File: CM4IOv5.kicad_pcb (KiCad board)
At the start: 4 copper layers, 115.1 x 56 mm, 120 parts, among them J1 Conn_01x02, J10 HDMI_C_1.4, J11 HDMI_C_1.4, J13 Conn_01x03, J14 Conn_01x03, J15 Audio OUT, J16 Micro_SD_Card_Det, J17 THD-20-R, J2 Bus_M.2_Socket_B, J3 USB_OTG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

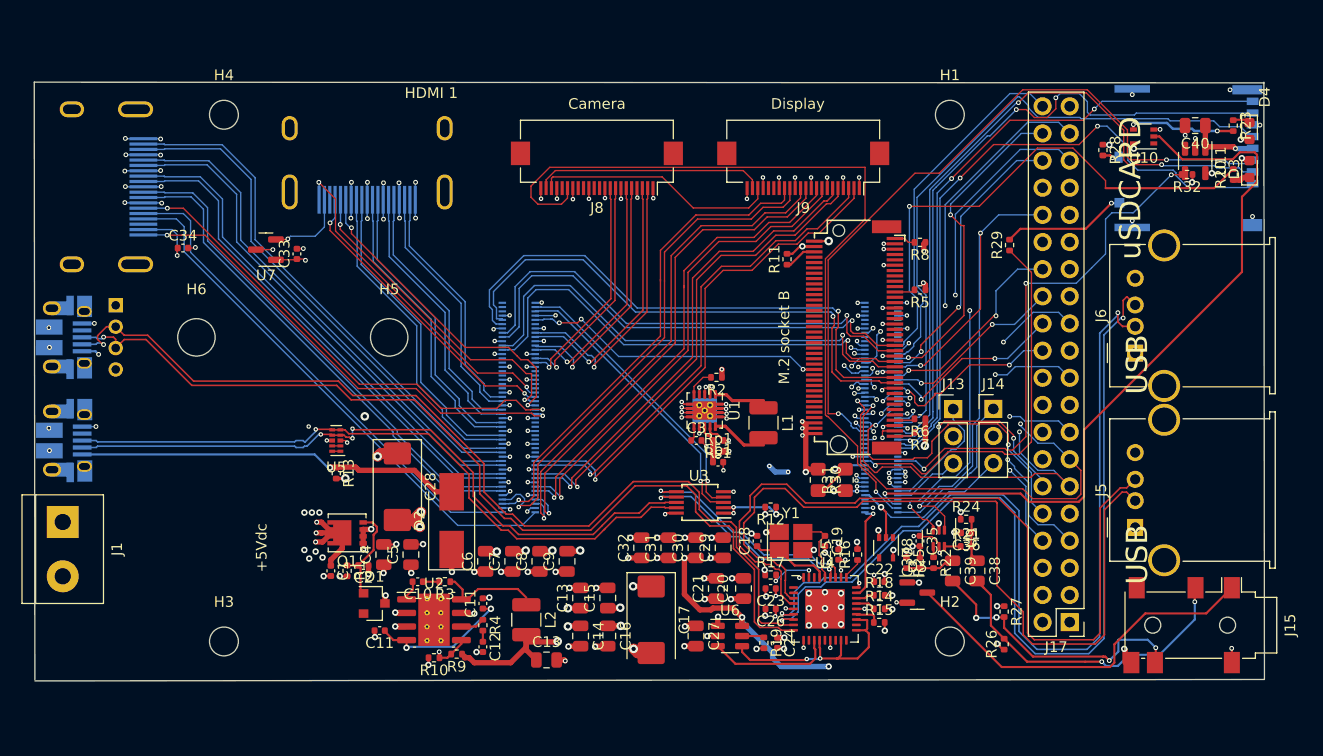
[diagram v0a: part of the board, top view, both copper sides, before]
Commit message: Completed initial routing
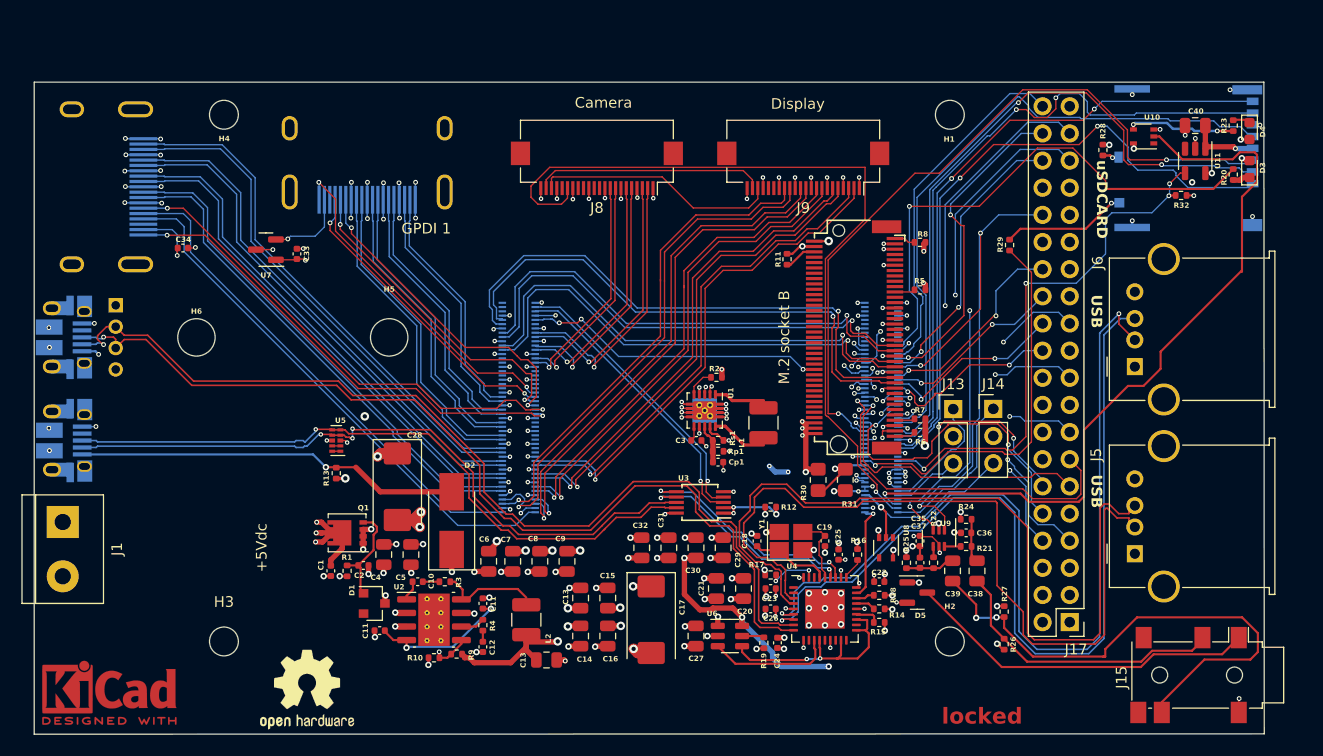
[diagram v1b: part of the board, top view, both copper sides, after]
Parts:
- added REF**: OSHW-Logo2_9.8x8mm_SilkScreen, Symbol:OSHW-Logo2_9.8x8mm_SilkScreen, F.Cu at (122.3, 135.8)
- added REF**: KiCad-Logo2_5mm_Copper, Symbol:KiCad-Logo2_5mm_Copper, F.Cu at (103.8, 136.1)
- moved J15 4.71 mm to (204.8, 134.4)
- moved J5 2.46 mm to (199.8, 123.1)
- moved R32 2.04 mm to (204.1, 89.6)
- moved J6 1.27 mm to (199.8, 105.6)
- moved C6 0.29 mm to (139.3, 123.8)
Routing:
- net /CM4_GPIO (GPIO, SDCARD)/AUDIO_R: track 26.7 -> 49.1 mm, vias 4 -> 2
- net /CM4_GPIO (GPIO, SDCARD)/GPIO17: track 35.2 -> 27.3 mm, vias 2 -> 1
- net /CM4_GPIO (GPIO, SDCARD)/GPIO27: track 38.8 -> 32.8 mm, vias 2 -> 1
- net /+3.3v: track 327.0 -> 322.7 mm, vias 36 -> 37
- net /CM4_GPIO (GPIO, SDCARD)/AUDIO_L: track 31.0 -> 27.9 mm, vias 2 -> 0
- net (no net): track 2.65 -> 0.00 mm
- net Net-(D5-K): track 35.5 -> 33.2 mm
- net /USB2-HUB/HD3_P: track 84.3 -> 82.2 mm, vias 2 -> 1
- net /USB2-HUB/VBUS: track 165.0 -> 162.9 mm
- net /CM4_GPIO (GPIO, SDCARD)/SD_PWR_ON: track 49.1 -> 50.6 mm, vias 3 -> 4
- net /CM4_GPIO (GPIO, SDCARD)/nPWR_LED: track 70.5 -> 71.5 mm
- net /CM4_GPIO (GPIO, SDCARD)/SYNC_IN: track 0.94 -> 0.00 mm, vias 1 -> 0
- net Net-(D2-A): track 36.6 -> 36.1 mm
- net GND: track 184.1 -> 184.2 mm, vias 203 -> 193
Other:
- board size 115.1 x 56 mm -> 115.1 x 61 mm
- board text added: "GPDI 1"
- board text added: "locked"
- board text removed: "HDMI 1"

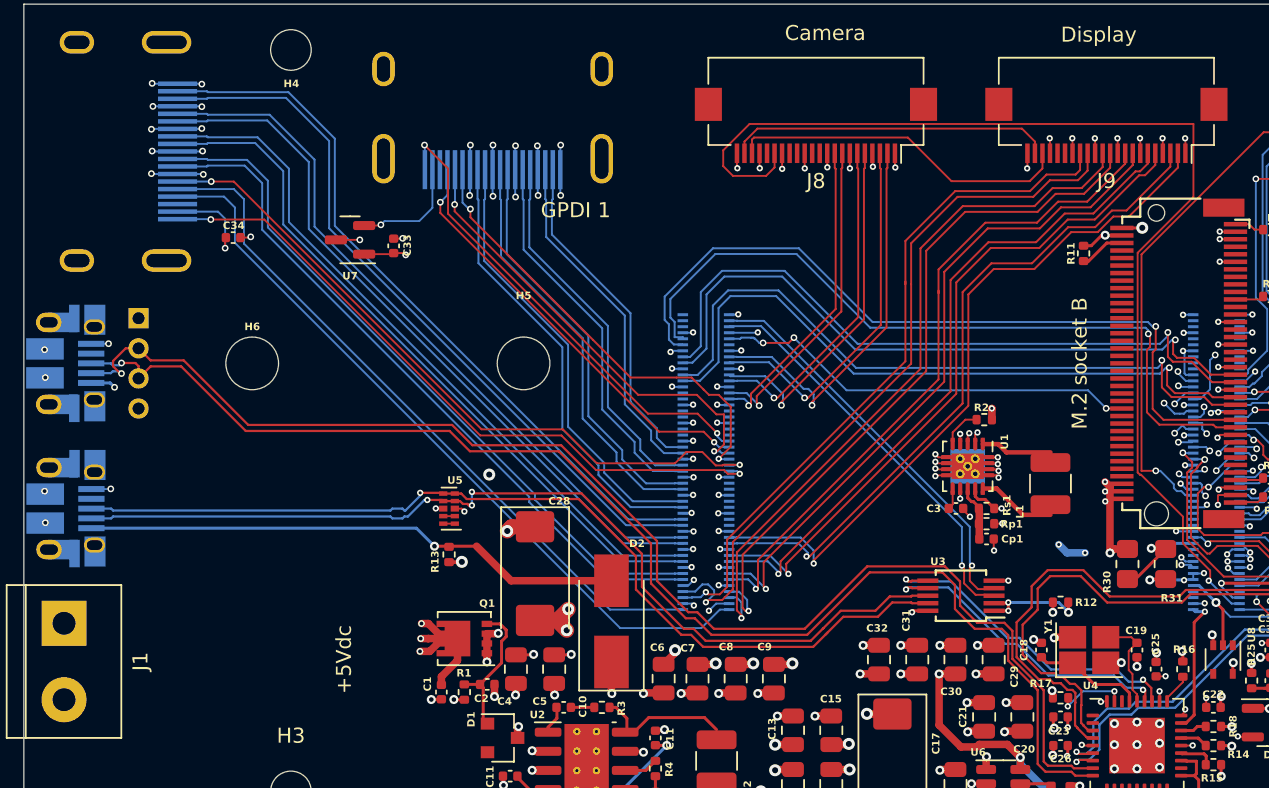
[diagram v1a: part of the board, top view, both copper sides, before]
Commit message: Tuning differential signals
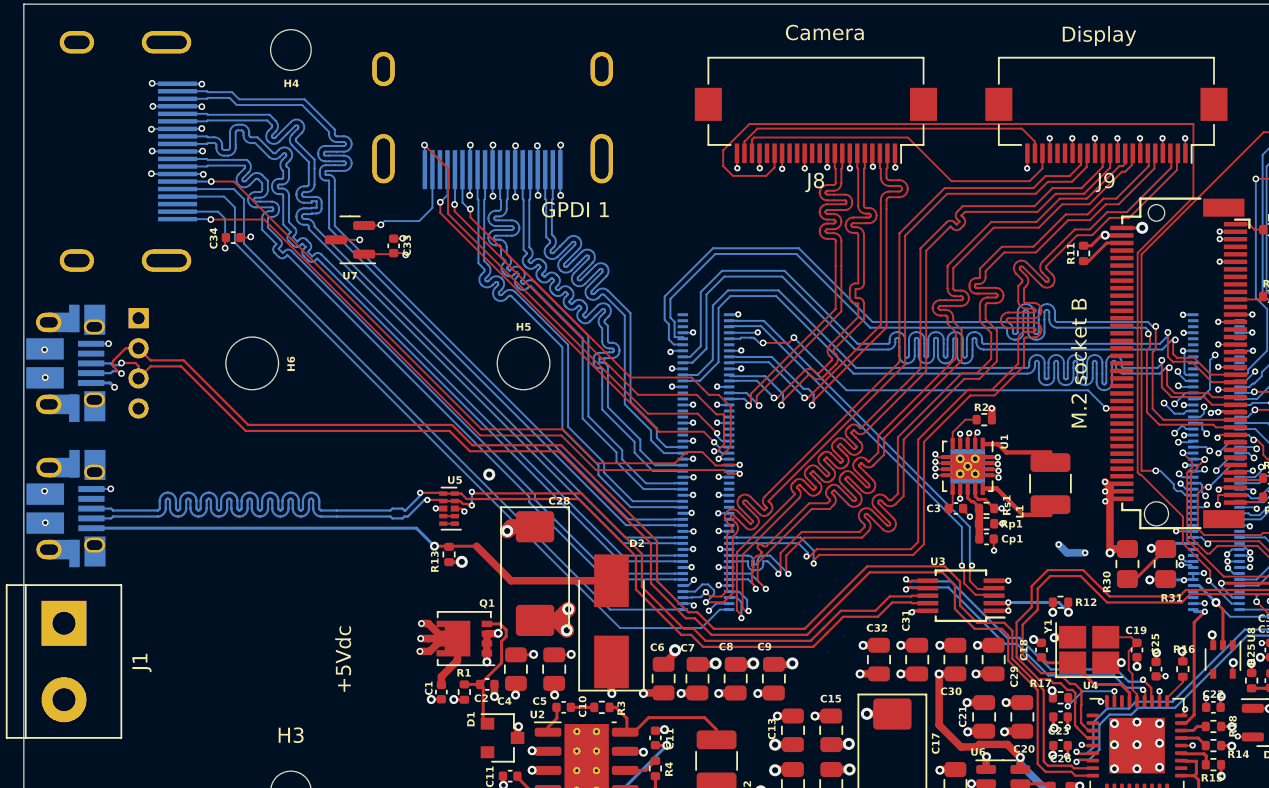
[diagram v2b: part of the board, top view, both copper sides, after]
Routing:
- net /USB2-HUB/USBD_P: track 63.3 -> 77.2 mm
- net /USB2-HUB/USBD_N: track 63.9 -> 77.8 mm
- net /CM4_HighSpeed/DSI1_D0_N: track 47.4 -> 59.8 mm
- net /CM4_HighSpeed/DSI1_C_P: track 44.6 -> 57.0 mm
- net /PCIE_TX_P: track 45.9 -> 58.3 mm
- net /PCIE_TX_N: track 45.2 -> 57.6 mm
- net /CM4_HighSpeed/DSI1_D0_P: track 45.9 -> 58.3 mm
- net /PCIE_RX_N: track 45.2 -> 57.5 mm
- net /PCIE_RX_P: track 46.0 -> 58.3 mm
- net /CM4_HighSpeed/DSI1_C_N: track 45.2 -> 57.0 mm
- net /CM4_HighSpeed/DSI1_D1_P: track 45.0 -> 56.5 mm
- net /CM4_HighSpeed/HDMI1_D2_P: track 22.7 -> 34.2 mm
- net /CM4_HighSpeed/HDMI1_D2_N: track 23.4 -> 34.8 mm
- net /CM4_HighSpeed/DSI1_D1_N: track 45.8 -> 57.2 mm
- net /CM4_HighSpeed/DSI1_D2_N: track 46.9 -> 57.4 mm
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
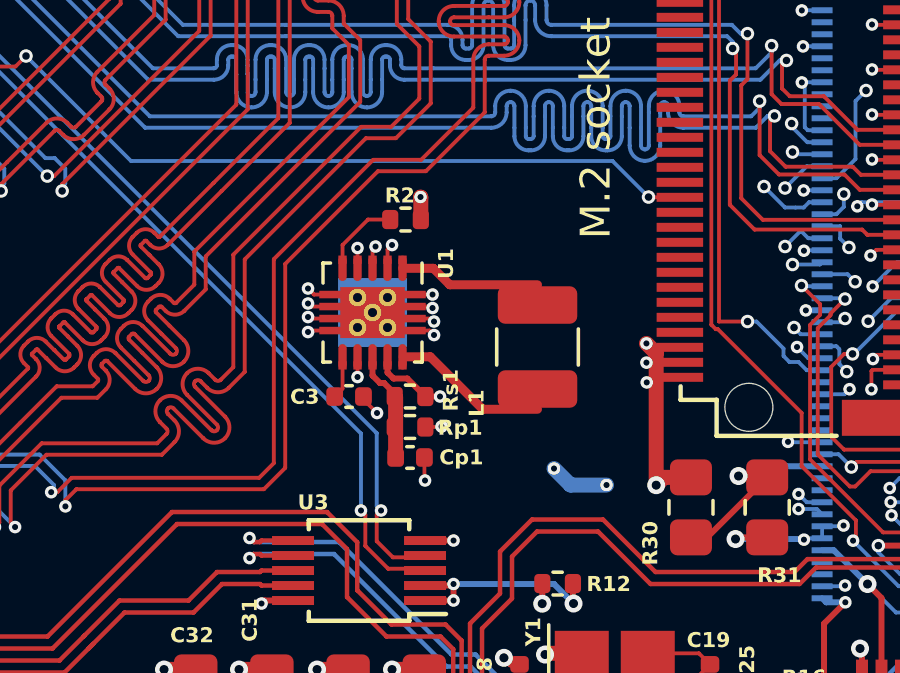
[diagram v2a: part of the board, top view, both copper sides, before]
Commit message: Removing U1
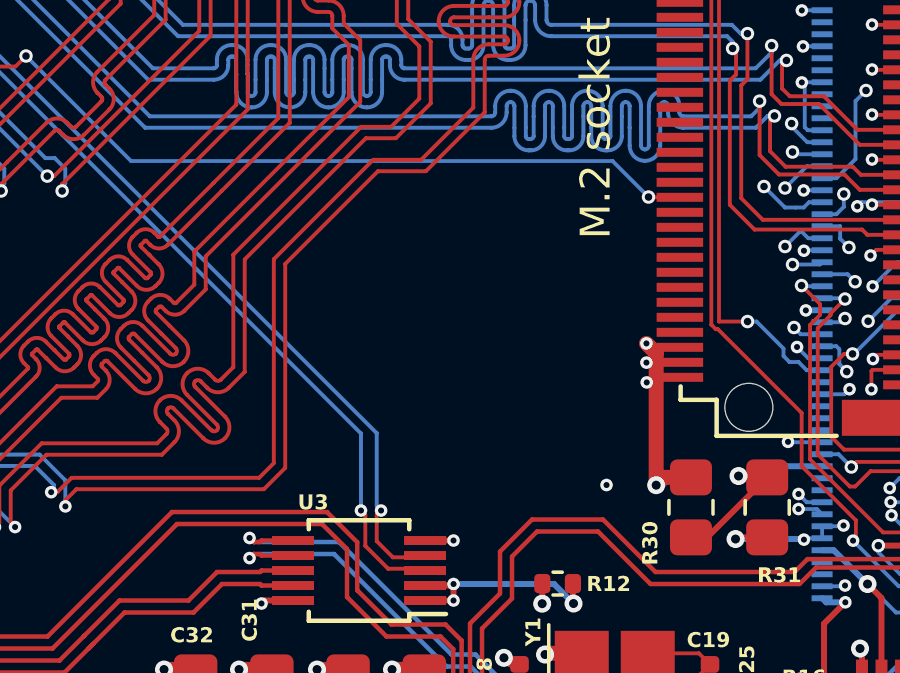
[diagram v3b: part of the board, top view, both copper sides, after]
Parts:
- removed C3: 100n, Capacitor_SMD:C_0402_1005Metric
- removed Cp1: 10pF, Capacitor_SMD:C_0402_1005Metric
- removed L1: SRN6045TA-1R0Y (1.0uH), Inductor_SMD:L_1210_3225Metric
- removed R2, Rs1: 1M 1%, Resistor_SMD:R_0402_1005Metric
- removed Rp1: 111K 1%, Resistor_SMD:R_0402_1005Metric
- removed U1: TPS63060DSC (adj), Package_SON:Texas_S-PWSON-N10_ThermalVias
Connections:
- U8 pad 4: Net-(J12-Pin_13) -> unconnected-(U8-Pad4)
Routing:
- net /+5v: track 238.7 -> 213.6 mm, vias 27 -> 24
- net /+3.3vSSD: track 118.3 -> 100.0 mm, vias 11 -> 9
- net GND: track 184.2 -> 175.2 mm, vias 193 -> 180
- net Net-(U1-L2): track 5.20 -> 0.00 mm
- net Net-(U1-L1): track 4.73 -> 0.00 mm
- net Net-(U1-FB): track 3.47 -> 0.00 mm
- net Net-(U1-PG): track 2.72 -> 0.00 mm
- net Net-(U1-VAUX): track 1.43 -> 0.00 mm

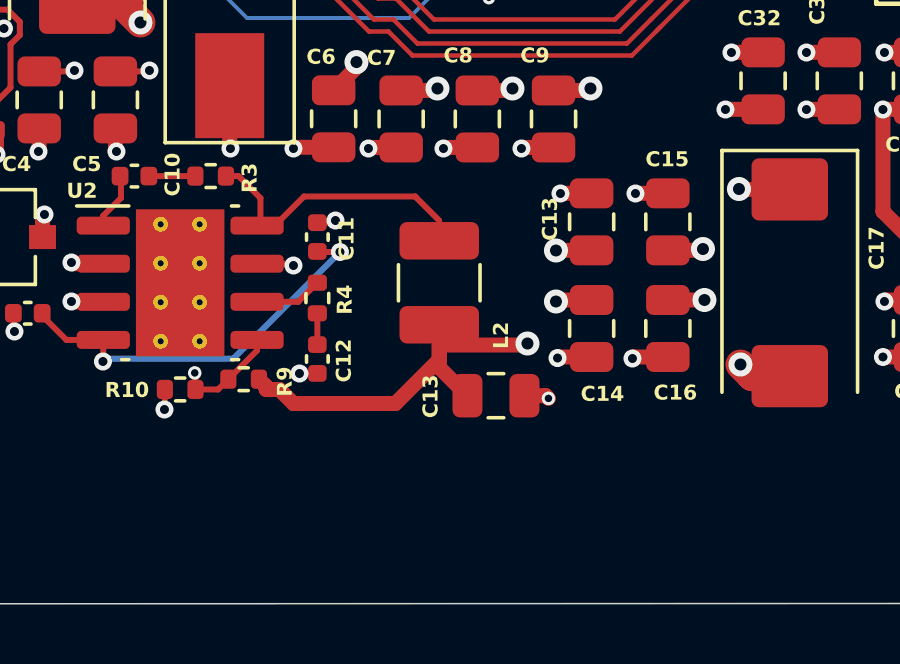
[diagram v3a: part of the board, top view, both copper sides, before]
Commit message: Changing L2
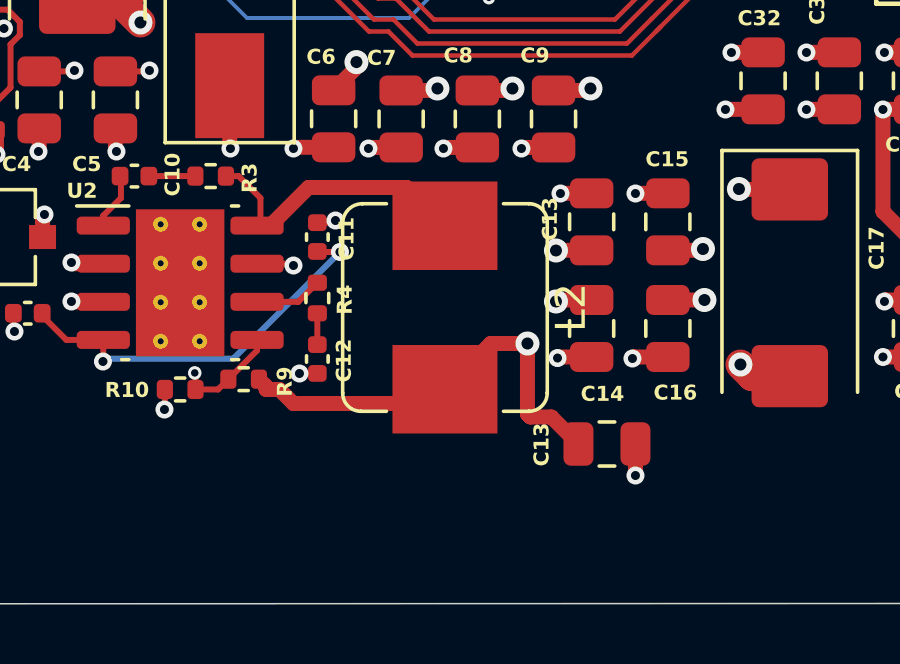
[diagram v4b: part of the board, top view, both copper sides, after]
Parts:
- L2: footprint Inductor_SMD:L_1210_3225Metric -> Inductor_SMD:L_Bourns_SRP7028A_7.3x6.6mm
- moved C13 4.04 mm to (148.4, 134.7)
- moved L2 0.85 mm to (143.1, 130.1)
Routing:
- net /+3.3vSSD: track 100.0 -> 101.5 mm
- net Net-(U2-SW): track 9.23 -> 10.3 mm
